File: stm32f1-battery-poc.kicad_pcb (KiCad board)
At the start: 4 copper layers, 92.5 x 85 mm, 153 parts, among them J1 Conn_01x02, J10 Conn_02x03_Odd_Even, J11 Conn_02x03_Odd_Even, J12 Conn_02x03_Odd_Even, J2 Conn_02x02_Odd_Even, J3 Conn_02x03_Odd_Even, J4 Conn_02x07_Odd_Even, J5 Conn_02x02_Odd_Even, J6 Conn_02x02_Odd_Even, J7 Conn_02x03_Odd_Even, J8 Conn_01x02, J9 Conn_01x04_Pin, M1 Stepper_Motor_bipolar, M2 Motor_3_Phases, Q1 Q_NMOS, Q2 Q_NMOS, SW1 SW_Push, SW2 SW_Push, SW3 SW_Push, SW4 SW_SPST, U1 LM78M05, U10 DRV8311H, U2 HT753-1, U3 SN65HVD230, U4 QRE1113GR, U5 QRE1113GR, U6 QRE1113GR, U7 DRV8424RGER, U8 STM32F103C8Tx, U9 BQ77905, Y1 8M

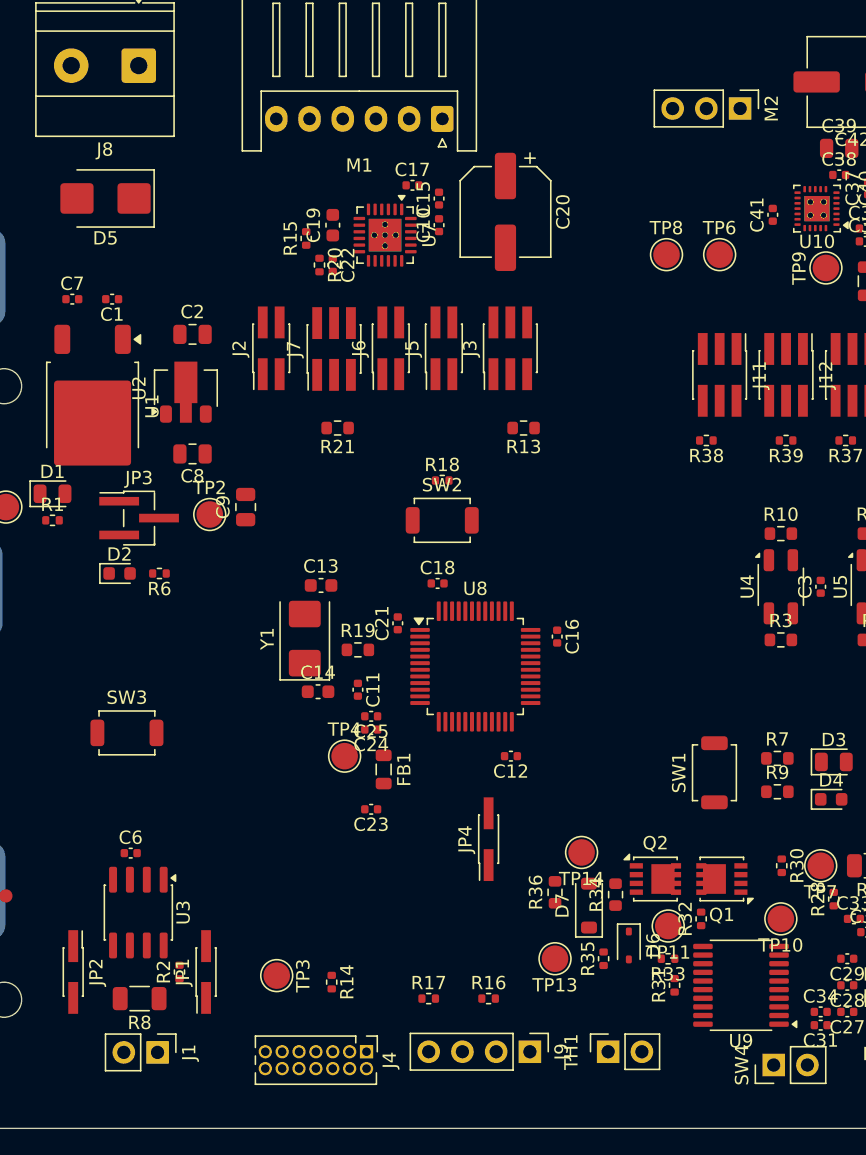
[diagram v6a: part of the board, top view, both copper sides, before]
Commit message: pcb: refine connectors positions
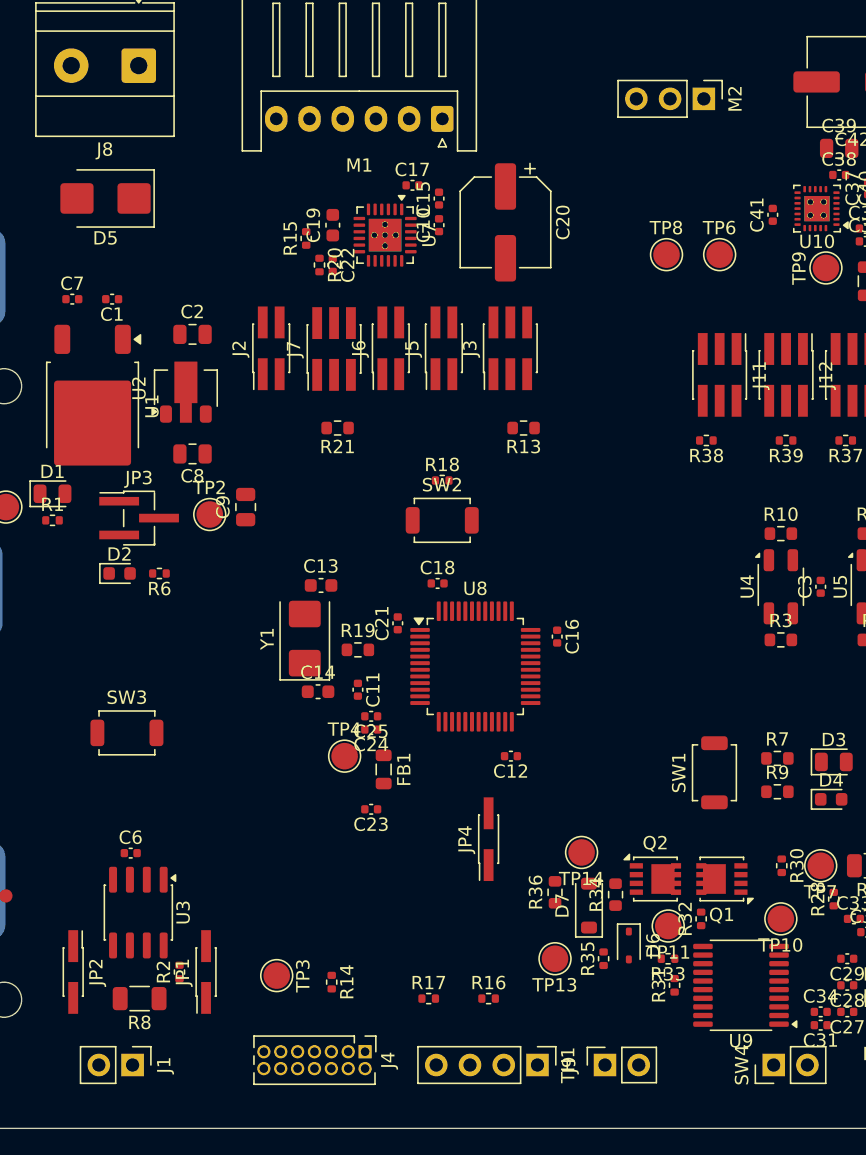
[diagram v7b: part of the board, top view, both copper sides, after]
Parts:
- moved M2 2.83 mm to (165.0, 50.0)
- moved J1 2.11 mm to (122.0, 122.7)
- moved J9 1.15 mm to (152.5, 122.7)
- moved TH1 1.03 mm to (157.6, 122.7)
- moved C20 0.79 mm to (150.1, 59.3)
- moved J4 0.11 mm to (139.5, 121.7)
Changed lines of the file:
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@@
 	(footprint "Connector_PinHeader_2.54mm:PinHeader_1x02_P2.54mm_Vertical"
 		(layer "F.Cu")
-		(at 123.9175 121.78 -90)
+		(at 122.0375 122.73 -90)
 		(descr "Through hole straight pin header, 1x02, 2.54mm pitch, single row")
 		(tags "Through hole pin header THT 1x02 2.54mm single row")
@@
 	(footprint "Connector_PinSocket_2.54mm:PinSocket_1x02_P2.54mm_Vertical"
 		(layer "F.Cu")
-		(at 157.8375 121.73 90)
+		(at 157.5975 122.73 90)
 		(descr "Through hole straight socket strip, 1x02, 2.54mm pitch, single row (from Kicad 4.0.7), script generated")
 		(tags "Through hole socket strip THT 1x02 2.54mm single row")
@@
 	(footprint "Connector_PinHeader_2.54mm:PinHeader_1x04_P2.54mm_Vertical"
 		(layer "F.Cu")
-		(at 151.9475 121.73 -90)
+		(at 152.5175 122.73 -90)
 		(descr "Through hole straight pin header, 1x04, 2.54mm pitch, single row")
 		(tags "Through hole pin header THT 1x04 2.54mm single row")
@@
 	(footprint "Capacitor_SMD:CP_Elec_6.3x7.7"
 		(layer "F.Cu")
-		(at 150.1075 58.51 -90)
+		(at 150.1075 59.3 -90)
 		(descr "SMD capacitor, aluminum electrolytic, Nichicon, 6.3x7.7mm")
 		(tags "capacitor electrolytic")
@@
 	(footprint "Connector_PinHeader_2.54mm:PinHeader_1x03_P2.54mm_Vertical"
 		(layer "F.Cu")
-		(at 167.77 50.73 -90)
+		(at 165.04 50 -90)
 		(descr "Through hole straight pin header, 1x03, 2.54mm pitch, single row")
 		(tags "Through hole pin header THT 1x03 2.54mm single row")
@@
 	(footprint "Connector_PinHeader_1.27mm:PinHeader_2x07_P1.27mm_Vertical"
 		(layer "F.Cu")
-		(at 139.6475 121.73 -90)
+		(at 139.54 121.73 -90)
 		(descr "Through hole straight pin header, 2x07, 1.27mm pitch, double rows")
 		(tags "Through hole pin header THT 2x07 1.27mm double row")
